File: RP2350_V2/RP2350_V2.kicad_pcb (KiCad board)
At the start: 4 copper layers, 68.9 x 116.2 mm, 148 parts, among them IC1 DMP1045U-7, IC2 DMP1045U-7, IC3 DMP1045U-7, IC4 DMP1045U-7, IC5 DMP1045U-7, IC6 DMP1045U-7, J1 Conn_01x04_Pin, J10 S0991-46R, J2 S0991-46R, J3 USB_C_Receptacle_USB2.0_16P, J4 RF_CONNECTOR_5-1814832-2, J5 Conn_01x08_Socket, J6 Conn_01x02_Pin, J7 Conn_01x04_Pin, J8 S0991-46R, J9 S0991-46R, SW1 PTS 647 SN50 SMTR2 LFS, SW10 PTS 647 SN50 SMTR2 LFS, SW11 PTS 647 SN50 SMTR2 LFS, SW12 PTS 647 SN50 SMTR2 LFS, SW13 PTS 647 SN50 SMTR2 LFS, SW14 PTS 647 SN50 SMTR2 LFS, SW4 PTS 647 SN50 SMTR2 LFS, SW9 PTS 647 SN50 SMTR2 LFS, U1 RP2350_60QFN, U2 W25Q128JVS, U3 TPS62811QWRWYRQ1, U4 MCP73812T-420I-OT, U5 TLV3012AIDCKR, U6 74HC14, X1 ABM8-272-T3

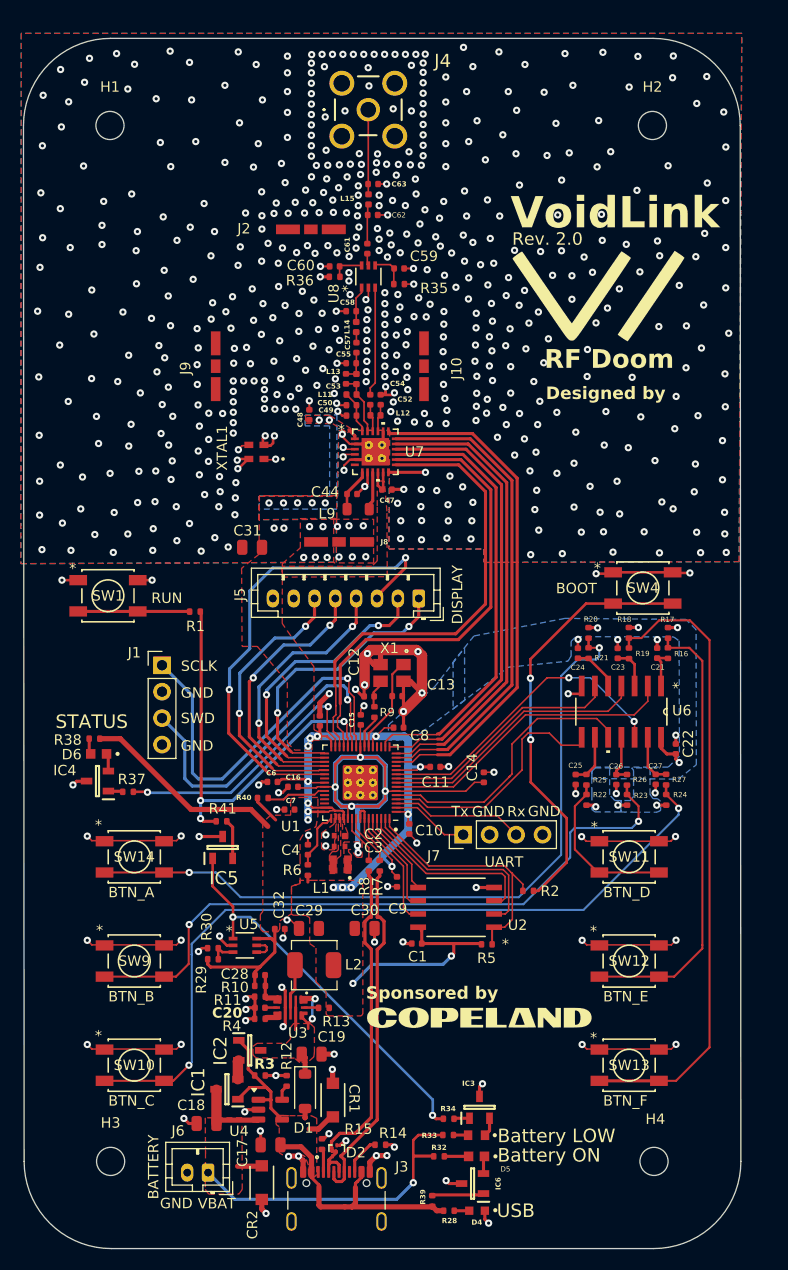
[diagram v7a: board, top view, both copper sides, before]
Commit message: fixed RF impedance matched width, changed rf connector, etc.
DRC+DFM clean with waivers. Pending final review for tapeout.
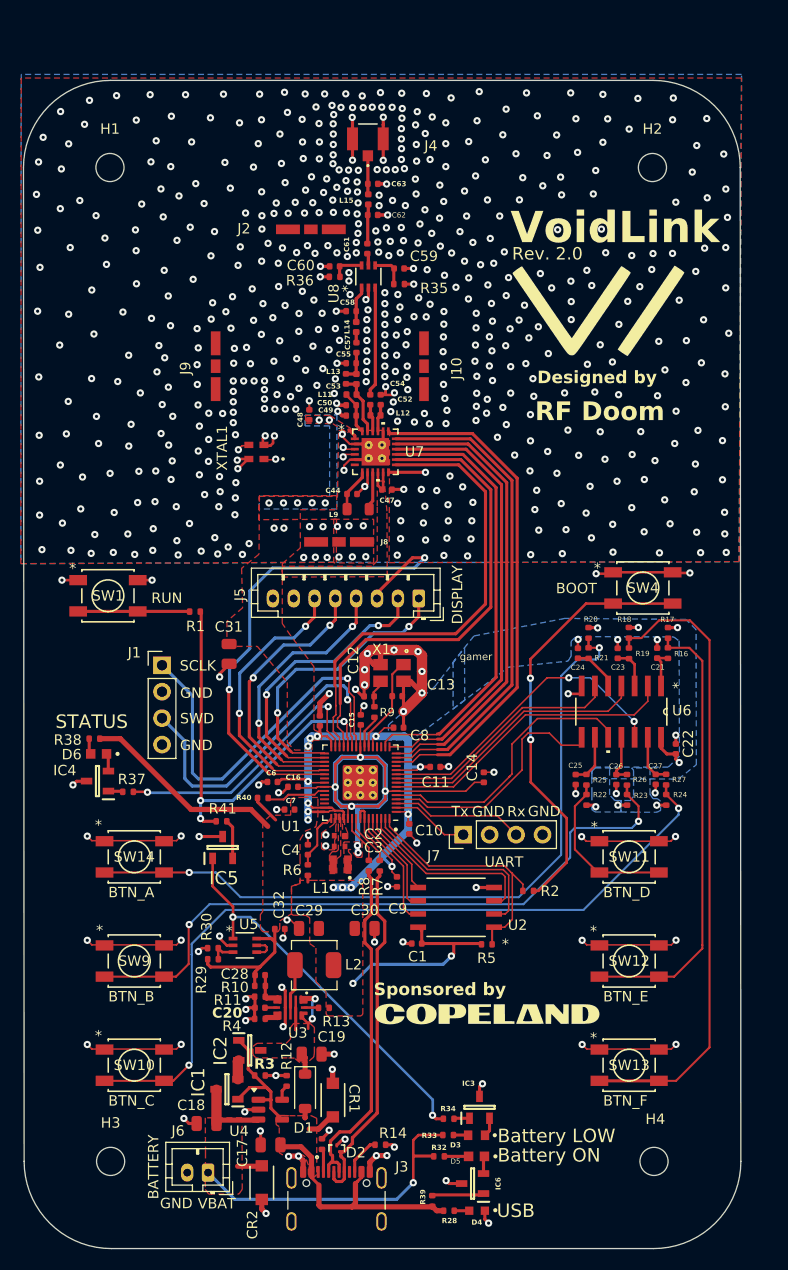
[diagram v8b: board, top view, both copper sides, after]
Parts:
- D3: value LTST-C190KRKT -> LTW-C193DS5-ND
- D5: value LTST-C191KFKT -> LTST-C193TGKT-5A
- J4: value RF_CONNECTOR_5-1814832-2 -> IPEX1; footprint My_Footprints:RF_CONNECTOR_518148322 -> My_Footprints:MHF I_RECE_IPX
- R33: value 88.7 -> 20
- moved C31 10.5 mm to (131.6, 92.0), turned to -90 degrees
- moved H1 4.04 mm to (120.2, 45.3)
- moved H2 4.04 mm to (172.2, 45.3)
- moved J4 2.80 mm to (144.9, 42.6), turned to -90 degrees
- moved G*** 1.42 mm to (167.1, 59.1)
- moved G*** 0.83 mm to (156.4, 126.6)
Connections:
- net SPIO_CLK renamed SPI0_CLK
- J4 pad 1: Net-(C63-Pad2) -> GND
- J4 pad 3: GND -> Net-(C63-Pad2)
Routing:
- net GND: track 192.2 -> 202.2 mm, vias 637 -> 654
- net Net-(C63-Pad2): track 8.15 -> 3.92 mm
- net /DISPLAY_DC: track 46.7 -> 49.9 mm
- net /USB_D-: track 35.4 -> 33.5 mm
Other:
- board size 68.9 x 116.2 mm -> 68.9 x 112.1 mm
- board text added: "gamer"
